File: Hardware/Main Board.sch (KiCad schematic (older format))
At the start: 17 parts, among them U1 SN75176BDR, U1 STM32F401RCT6, X1 24MHz

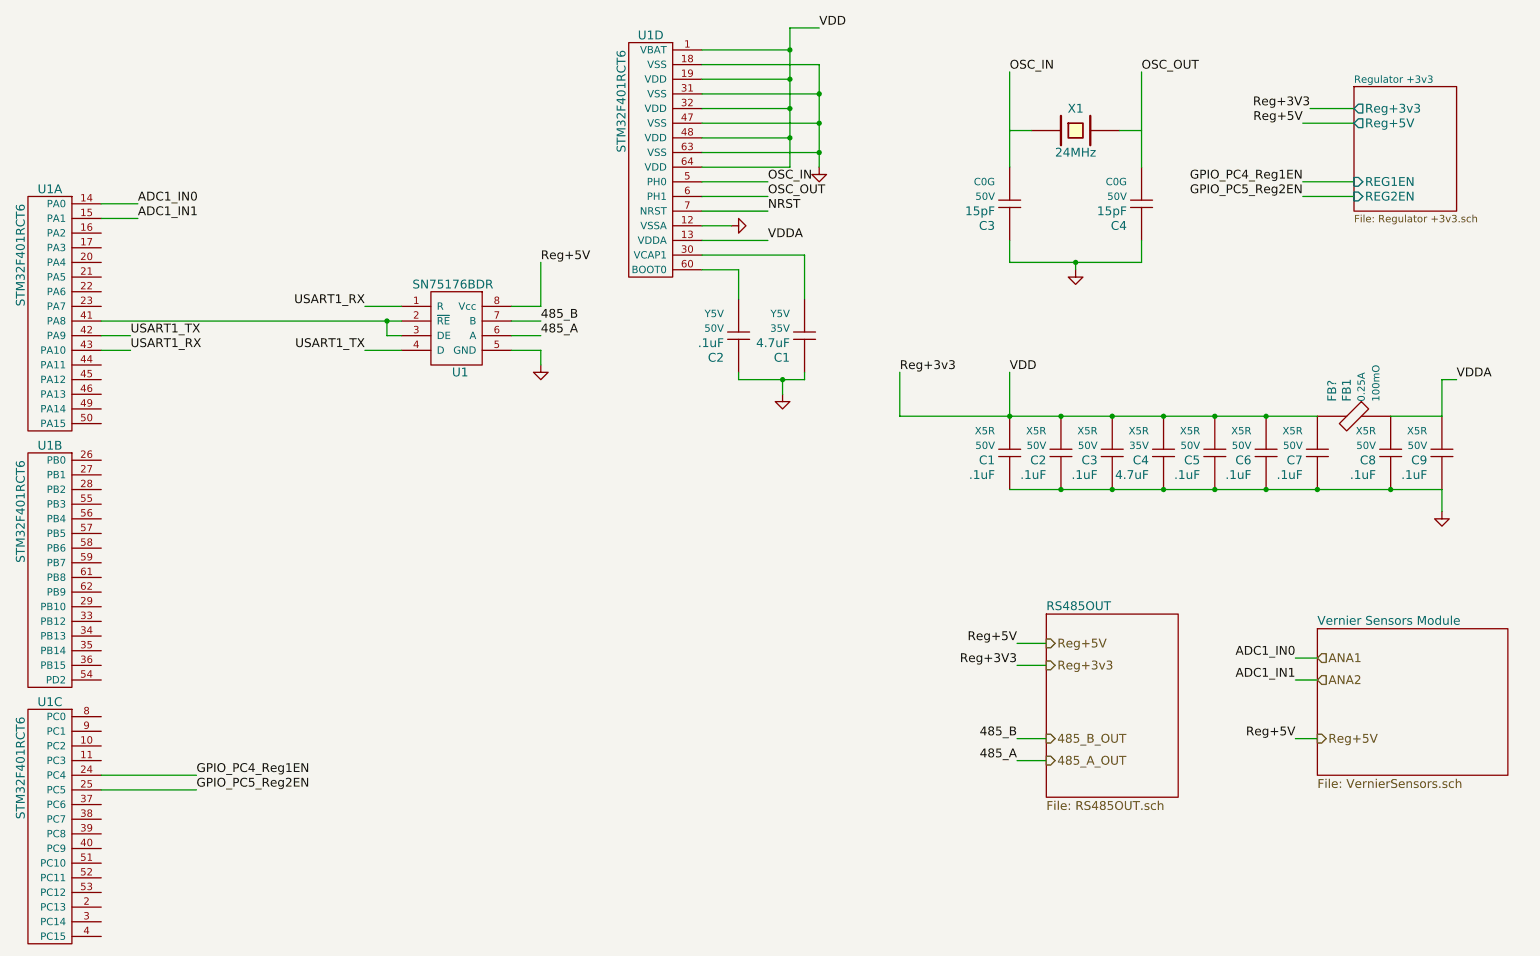
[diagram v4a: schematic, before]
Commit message: Add instrumentation amplifier for load cell, added amplifiers for ph and moisture sensors
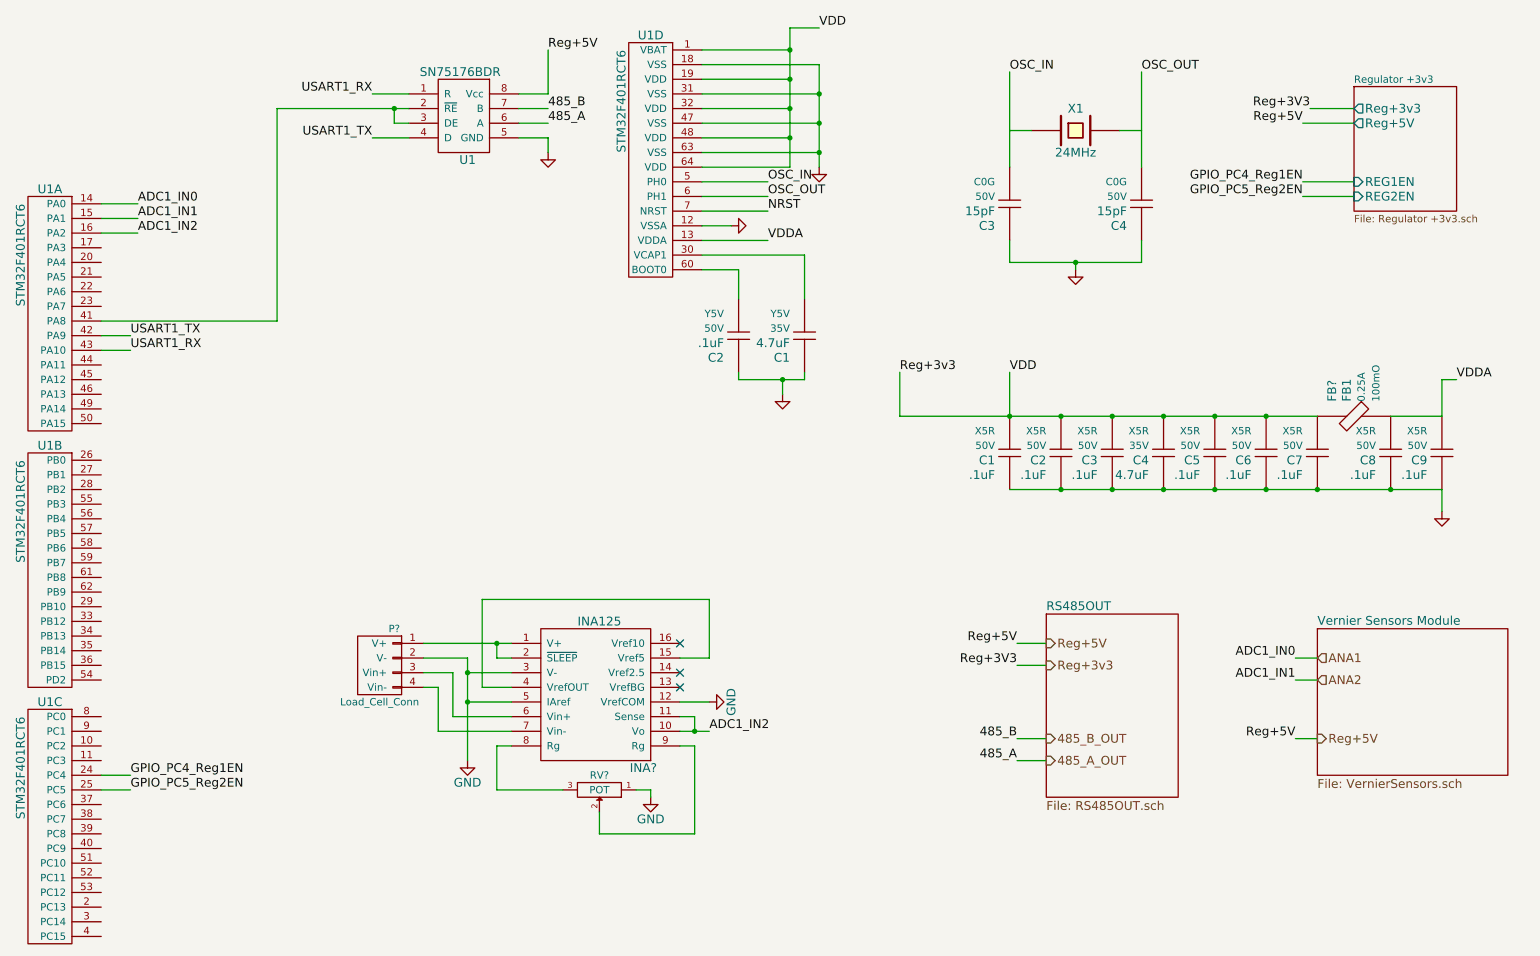
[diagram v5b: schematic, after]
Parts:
- added INA?: INA125, symbol INA125
- added P?: Load_Cell_Conn, symbol Load_Cell_Conn
- added RV?: POT, symbol POT
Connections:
- net GND: now also INA?.12 (VrefCOM), INA?.3 (V-), INA?.5 (IAref), P?.2 (V-), RV?.1
- net ADC1_IN2: now reaches U1.16 (PA2)
- net ADC1_IN2: now also INA?.10 (Vo), INA?.11 (Sense)
- new net: INA?.1 (V+), INA?.2 (~SLEEP), P?.1 (V+)
- new net: INA?.15 (Vref5), INA?.4 (VrefOUT)
- new net: INA?.6 (Vin+), P?.3 (Vin+)
- new net: INA?.7 (Vin-), P?.4 (Vin-)
- new net: INA?.8 (Rg), RV?.3
- new net: INA?.9 (Rg), RV?.2
- no-connect marks 0 -> 3
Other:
- moved on the sheet: U1

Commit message: Fix capacitor annotation problem
The capacitors from the same library were assigned the same numbers for
an unknown reason.
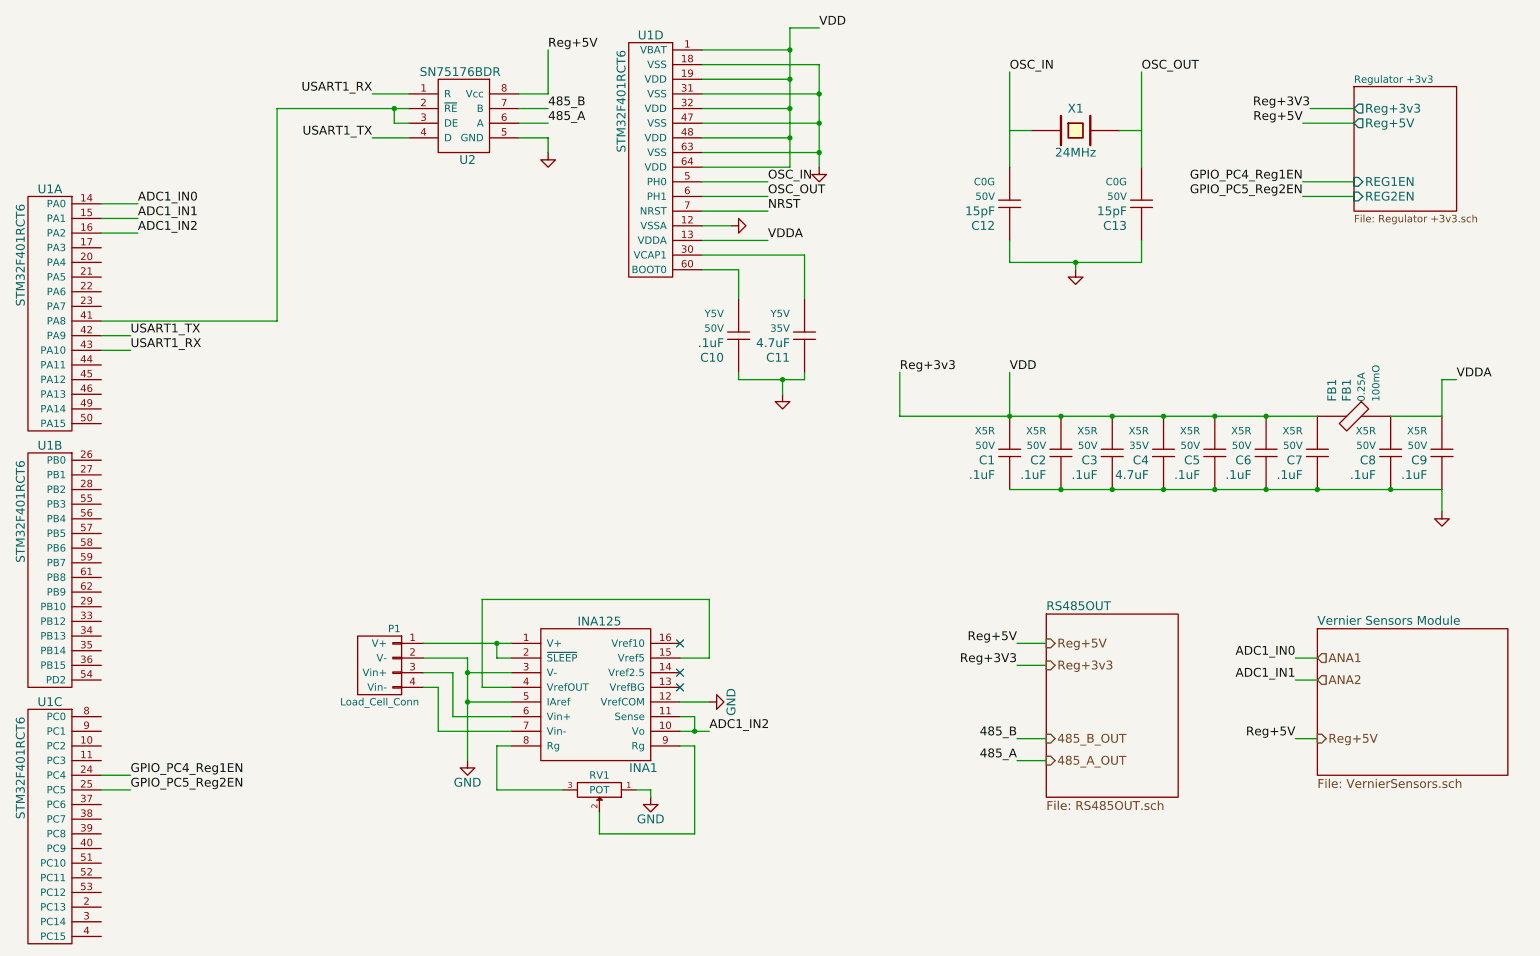
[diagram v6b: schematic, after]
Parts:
- gave numbers to parts that had none: 4
- renumbered C2 to C10, C1 to C11, C3 to C12, C4 to C13, U1 to U2
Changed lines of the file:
@@
 $EndComp
 $Comp
-L Ferrite FB?
+L Ferrite FB1
 U 1 1 54E8BEB9
 P 9750 3250
-F 0 "FB?" V 9600 3350 60  0000 L CNN
+F 0 "FB1" V 9600 3350 60  0000 L CNN
 F 1 "FB1" V 9700 3350 60  0000 L CNN
 F 2 "" H 9650 3250 60  0001 C CNN
@@
 Reg+3v3
 $Comp
-L GND #PWR?
+L GND #PWR7
 U 1 1 54E8FDC8
 P 6100 1550
-F 0 "#PWR?" H 6100 1550 30  0001 C CNN
+F 0 "#PWR7" H 6100 1550 30  0001 C CNN
 F 1 "GND" H 6100 1480 30  0001 C CNN
 F 2 "" H 6100 1550 60  0000 C CNN
@@
 VDD
 $Comp
-L GND #PWR?
+L GND #PWR5
 U 1 1 54E8FF26
 P 5500 1950
-F 0 "#PWR?" H 5500 1950 30  0001 C CNN
+F 0 "#PWR5" H 5500 1950 30  0001 C CNN
 F 1 "GND" H 5500 1880 30  0001 C CNN
 F 2 "" H 5500 1950 60  0000 C CNN
@@
 $EndComp
 $Comp
-L Capacitor C1
+L Capacitor C11
 U 1 1 54E8FFCC
 P 6000 2700
-F 0 "C1" V 5850 2800 60  0000 L CNN
+F 0 "C11" V 5850 2800 60  0000 L CNN
 F 1 "4.7uF" V 5950 2800 60  0000 L CNN
 F 2 "" H 5900 2700 60  0001 C CNN
@@
 $EndComp
 $Comp
-L GND #PWR?
+L GND #PWR6
 U 1 1 54E9002D
 P 5850 3100
-F 0 "#PWR?" H 5850 3100 30  0001 C CNN
+F 0 "#PWR6" H 5850 3100 30  0001 C CNN
 F 1 "GND" H 5850 3030 30  0001 C CNN
 F 2 "" H 5850 3100 60  0000 C CNN
@@
 NRST
 $Comp
-L Capacitor C2
+L Capacitor C10
 U 1 1 54E902D3
 P 5550 2700
-F 0 "C2" V 5400 2800 60  0000 L CNN
+F 0 "C10" V 5400 2800 60  0000 L CNN
 F 1 ".1uF" V 5500 2800 60  0000 L CNN
 F 2 "" H 5450 2700 60  0001 C CNN
@@
 $EndComp
 $Comp
-L Capacitor C3
+L Capacitor C12
 U 1 1 54E90815
 P 7400 1800
-F 0 "C3" V 7250 1900 60  0000 L CNN
+F 0 "C12" V 7250 1900 60  0000 L CNN
 F 1 "15pF" V 7350 1900 60  0000 L CNN
 F 2 "" H 7300 1800 60  0001 C CNN
@@
 $EndComp
 $Comp
-L Capacitor C4
+L Capacitor C13
 U 1 1 54E9089F
 P 8300 1800
-F 0 "C4" V 8150 1900 60  0000 L CNN
+F 0 "C13" V 8150 1900 60  0000 L CNN
 F 1 "15pF" V 8250 1900 60  0000 L CNN
 F 2 "" H 8200 1800 60  0001 C CNN
@@
 $EndComp
 $Comp
-L GND #PWR?
+L GND #PWR8
 U 1 1 54E90BC2
 P 7850 2250
-F 0 "#PWR?" H 7850 2250 30  0001 C CNN
+F 0 "#PWR8" H 7850 2250 30  0001 C CNN
 F 1 "GND" H 7850 2180 30  0001 C CNN
 F 2 "" H 7850 2250 60  0000 C CNN
@@
 Reg+3V3
 $Comp
-L GND #PWR?
+L GND #PWR9
 U 1 1 54E91751
 P 10350 3900
-F 0 "#PWR?" H 10350 3900 30  0001 C CNN
+F 0 "#PWR9" H 10350 3900 30  0001 C CNN
 F 1 "GND" H 10350 3830 30  0001 C CNN
 F 2 "" H 10350 3900 60  0000 C CNN
@@
 $EndSheet
 $Comp
-L SN75176BDR U1
+L SN75176BDR U2
 U 1 1 54FB3511
 P 3850 1050
-F 0 "U1" H 3700 600 60  0000 C CNN
+F 0 "U2" H 3700 600 60  0000 C CNN
 F 1 "SN75176BDR" H 3650 1200 60  0000 C CNN
 F 2 "" H 3850 1050 60  0000 C CNN
@@
 USART1_RX
 $Comp
-L GND #PWR?
+L GND #PWR2
 U 1 1 54FB679B
 P 4250 1450
-F 0 "#PWR?" H 4250 1450 30  0001 C CNN
+F 0 "#PWR2" H 4250 1450 30  0001 C CNN
 F 1 "GND" H 4250 1380 30  0001 C CNN
 F 2 "" H 4250 1450 60  0000 C CNN
@@
 $EndSheet
 $Comp
-L INA125 INA?
+L INA125 INA1
 U 1 1 553293FE
 P 4600 5150
-F 0 "INA?" H 4900 4650 60  0000 C CNN
+F 0 "INA1" H 4900 4650 60  0000 C CNN
 F 1 "INA125" H 4600 5650 60  0000 C CNN
 F 2 "" H 4600 4700 60  0000 C CNN
@@
 ADC1_IN2
 $Comp
-L GND #PWR?
+L GND #PWR4
 U 1 1 55346924
 P 5350 5200
-F 0 "#PWR?" H 5350 4950 60  0001 C CNN
+F 0 "#PWR4" H 5350 4950 60  0001 C CNN
 F 1 "GND" H 5350 5050 60  0000 C CNN
 F 2 "" H 5350 5200 60  0000 C CNN
@@
 Connection ~ 3700 5200
 $Comp
-L GND #PWR?
+L GND #PWR1
 U 1 1 553493C3
 P 3700 5600
-F 0 "#PWR?" H 3700 5350 60  0001 C CNN
+F 0 "#PWR1" H 3700 5350 60  0001 C CNN
 F 1 "GND" H 3700 5450 60  0000 C CNN
 F 2 "" H 3700 5600 60  0000 C CNN
@@
 	3500 5100 3400 5100
 $Comp
-L Load_Cell_Conn P?
+L Load_Cell_Conn P1
 U 1 1 5534E679
 P 3200 5050
-F 0 "P?" H 3200 5400 50  0000 C CNN
+F 0 "P1" H 3200 5400 50  0000 C CNN
 F 1 "Load_Cell_Conn" H 3300 4900 50  0000 C CNN
 F 2 "" H 3200 5050 60  0000 C CNN
@@
 $EndComp
 $Comp
-L POT RV?
+L POT RV1
 U 1 1 55358BF8
 P 4600 5800
-F 0 "RV?" H 4600 5700 50  0000 C CNN
+F 0 "RV1" H 4600 5700 50  0000 C CNN
 F 1 "POT" H 4600 5800 50  0000 C CNN
 F 2 "" H 4600 5800 60  0000 C CNN
@@
 	4950 5800 4950 5850
 $Comp
-L GND #PWR?
+L GND #PWR3
 U 1 1 55366DC6
 P 4950 5850
-F 0 "#PWR?" H 4950 5600 60  0001 C CNN
+F 0 "#PWR3" H 4950 5600 60  0001 C CNN
 F 1 "GND" H 4950 5700 60  0000 C CNN
 F 2 "" H 4950 5850 60  0000 C CNN

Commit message: Fix annotation problem, Add IC datasheets
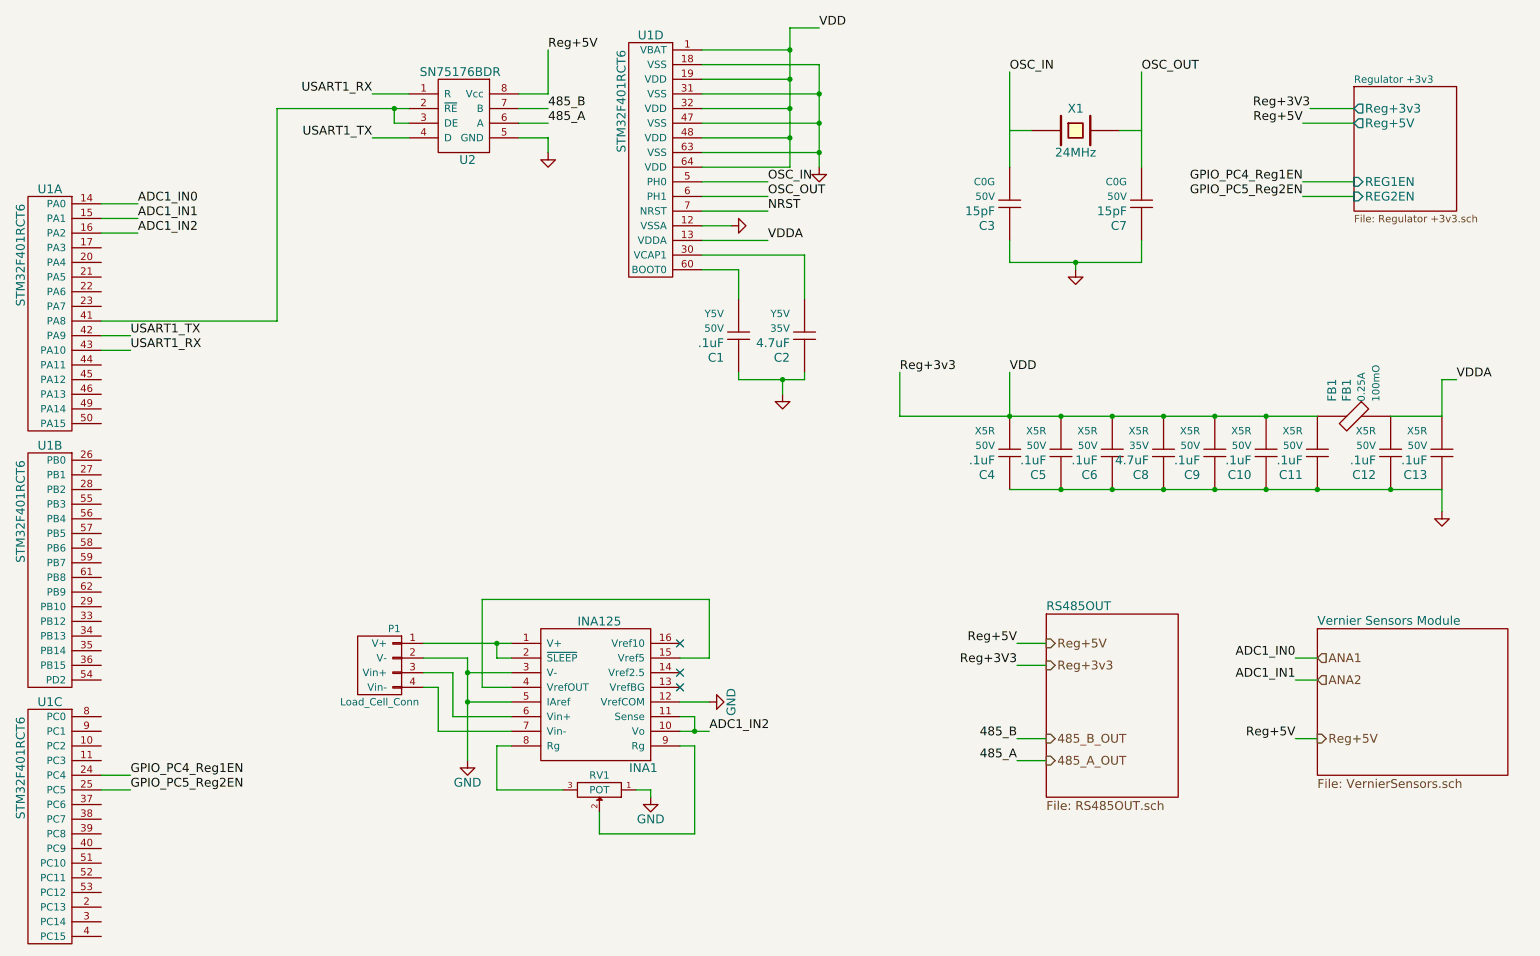
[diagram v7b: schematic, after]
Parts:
- removed .1uF: C5, symbol Capacitor
- removed .1uF: C6, symbol Capacitor
- removed .1uF: C7, symbol Capacitor
- removed .1uF: C3, symbol Capacitor
- removed .1uF: C2, symbol Capacitor
- removed .1uF: C8, symbol Capacitor
- removed .1uF: C9, symbol Capacitor
- added C1, C11, C12, C13, C5, C6, C9: .1uF, symbol Capacitor
- C10: Dielectric Y5V -> X5R
- C4: renamed from .1uF; value C1 -> .1uF
- C8: renamed from 4.7uF; value C4 -> 4.7uF
- renumbered C11 to C2, C12 to C3, C13 to C7
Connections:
- net GND: now also C1.1, C11.1, C12.1, C13.1, C5.1, C6.1, C9.1
- net Reg+3v3: now also C10.2, C11.2, C5.2, C6.2, C9.2
- net VDDA: now also C12.2, C13.2
- net at U1.60 (BOOT0): now also C1.2; no longer C10.2
